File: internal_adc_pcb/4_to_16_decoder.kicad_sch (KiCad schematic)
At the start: 6 parts, among them U11 SN74AHC138RGYR, U12 SN74AHC138RGYR, U13 SN74LVC1G14DCKR_C19829630

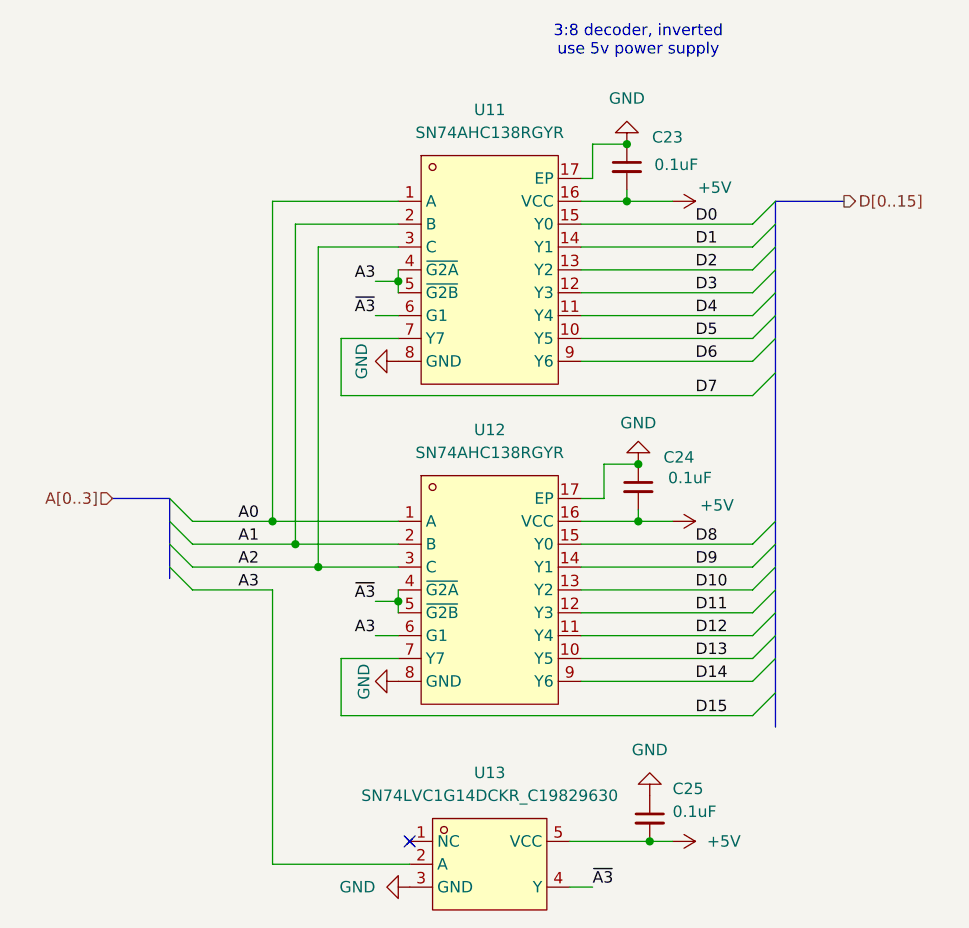
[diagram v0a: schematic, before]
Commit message: adjust VG issue for internal ADC version; changed naming for VG
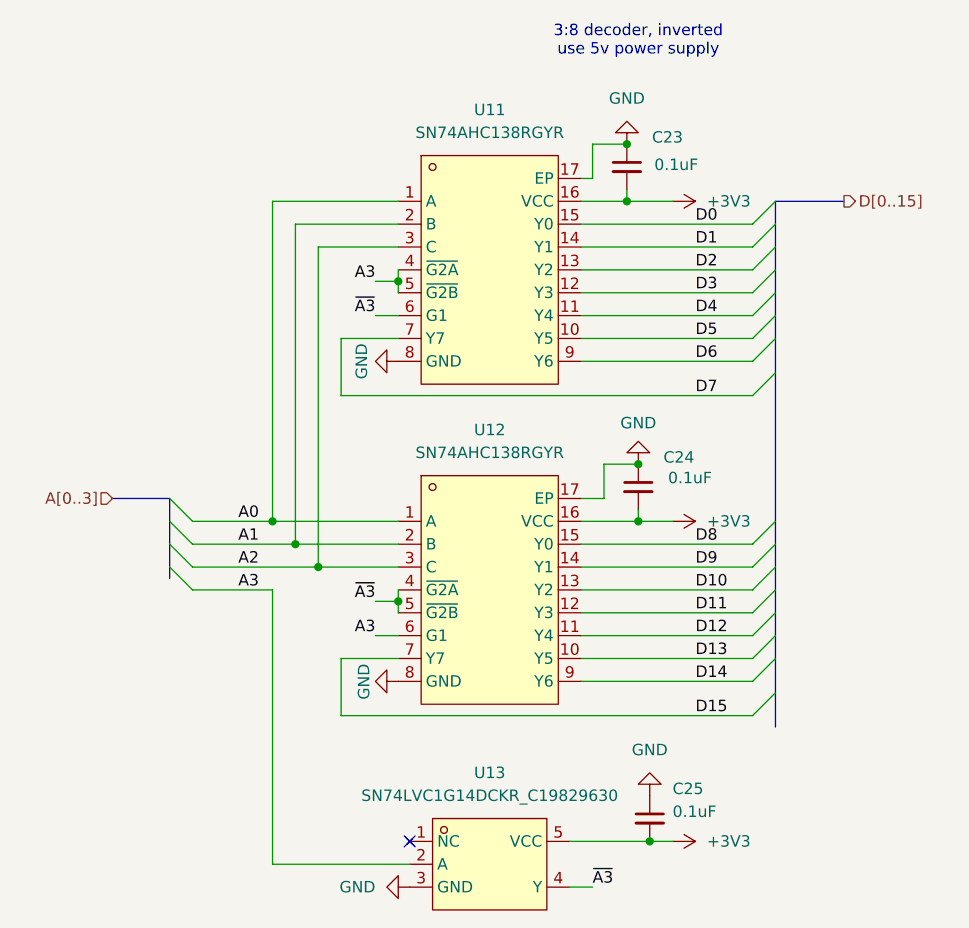
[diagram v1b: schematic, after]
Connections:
- net +5V renamed +3V3
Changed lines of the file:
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@@
 	)
 	(symbol
-		(lib_id "power:+5V")
-		(at 121.92 49.53 270)
-		(unit 1)
-		(body_style 1)
-		(exclude_from_sim no)
-		(in_bom yes)
-		(on_board yes)
-		(in_pos_files yes)
-		(dnp no)
-		(property "Reference" "#PWR065"
-			(at 118.11 49.53 0)
-			(hide yes)
-			(show_name no)
-			(do_not_autoplace no)
-			(effects
-				(font
-					(face "Iosevka NF")
-					(size 1.27 1.27)
-				)
-			)
-		)
-		(property "Value" "+5V"
-			(at 124.714 48.006 90)
-			(show_name no)
-			(do_not_autoplace no)
-			(effects
-				(font
-					(face "Iosevka NF")
+		(lib_id "power:+3V3")
+		(at 121.92 85.09 270)
+		(unit 1)
+		(body_style 1)
+		(exclude_from_sim no)
+		(in_bom yes)
+		(on_board yes)
+		(in_pos_files yes)
+		(dnp no)
+		(fields_autoplaced yes)
+		(property "Reference" "#PWR080"
+			(at 118.11 85.09 0)
+			(hide yes)
+			(show_name no)
+			(do_not_autoplace no)
+			(effects
+				(font
+					(size 1.27 1.27)
+				)
+			)
+		)
+		(property "Value" "+3V3"
+			(at 125.73 85.0899 90)
+			(show_name no)
+			(do_not_autoplace no)
+			(effects
+				(font
 					(size 1.27 1.27)
 				)
@@
 		)
 		(property "Footprint" ""
-			(at 121.92 49.53 0)
-			(hide yes)
-			(show_name no)
-			(do_not_autoplace no)
-			(effects
-				(font
-					(face "Iosevka NF")
-					(size 1.27 1.27)
-				)
-			)
-		)
-		(property "Datasheet" ""
-			(at 121.92 49.53 0)
-			(hide yes)
-			(show_name no)
-			(do_not_autoplace no)
-			(effects
-				(font
-					(face "Iosevka NF")
-					(size 1.27 1.27)
-				)
-			)
-		)
-		(property "Description" "Power symbol creates a global label with name \"+5V\""
-			(at 121.92 49.53 0)
-			(hide yes)
-			(show_name no)
-			(do_not_autoplace no)
-			(effects
-				(font
-					(face "Iosevka NF")
-					(size 1.27 1.27)
-				)
-			)
-		)
-		(pin "1"
-		)
-		(instances
-			(project "fsr_matrix_readout_external_adc"
-				(path "/6dca5e5c-f676-465d-98c9-14af6047a226/41800b67-536b-40f6-9870-7d633bd400f6"
-					(reference "#PWR02")
-					(unit 1)
-				)
-			)
-			(project "fsr_matrix_readout_internal_adc"
-				(path "/a2a8c34e-3adf-4a95-8857-b713f7048029/7bcd2658-0b6a-4321-9860-384b8d346995"
-					(reference "#PWR065")
+			(at 121.92 85.09 0)
+			(hide yes)
+			(show_name no)
+			(do_not_autoplace no)
+			(effects
+				(font
+					(size 1.27 1.27)
+				)
+			)
+		)
+		(property "Datasheet" ""
+			(at 121.92 85.09 0)
+			(hide yes)
+			(show_name no)
+			(do_not_autoplace no)
+			(effects
+				(font
+					(size 1.27 1.27)
+				)
+			)
+		)
+		(property "Description" "Power symbol creates a global label with name \"+3V3\""
+			(at 121.92 85.09 0)
+			(hide yes)
+			(show_name no)
+			(do_not_autoplace no)
+			(effects
+				(font
+					(size 1.27 1.27)
+				)
+			)
+		)
+		(pin "1"
+		)
+		(instances
+			(project "fsr_matrix_readout_internal_adc"
+				(path "/a2a8c34e-3adf-4a95-8857-b713f7048029/7bcd2658-0b6a-4321-9860-384b8d346995"
+					(reference "#PWR080")
 					(unit 1)
 				)
@@
 	)
 	(symbol
-		(lib_id "power:+5V")
-		(at 121.92 85.09 270)
-		(unit 1)
-		(body_style 1)
-		(exclude_from_sim no)
-		(in_bom yes)
-		(on_board yes)
-		(in_pos_files yes)
-		(dnp no)
-		(property "Reference" "#PWR066"
-			(at 118.11 85.09 0)
-			(hide yes)
-			(show_name no)
-			(do_not_autoplace no)
-			(effects
-				(font
-					(face "Iosevka NF")
-					(size 1.27 1.27)
-				)
-			)
-		)
-		(property "Value" "+5V"
-			(at 124.968 83.312 90)
-			(show_name no)
-			(do_not_autoplace no)
-			(effects
-				(font
-					(face "Iosevka NF")
-					(size 1.27 1.27)
-				)
-				(justify left)
-			)
-		)
-		(property "Footprint" ""
-			(at 121.92 85.09 0)
-			(hide yes)
-			(show_name no)
-			(do_not_autoplace no)
-			(effects
-				(font
-					(face "Iosevka NF")
-					(size 1.27 1.27)
-				)
-			)
-		)
-		(property "Datasheet" ""
-			(at 121.92 85.09 0)
-			(hide yes)
-			(show_name no)
-			(do_not_autoplace no)
-			(effects
-				(font
-					(face "Iosevka NF")
-					(size 1.27 1.27)
-				)
-			)
-		)
-		(property "Description" "Power symbol creates a global label with name \"+5V\""
-			(at 121.92 85.09 0)
-			(hide yes)
-			(show_name no)
-			(do_not_autoplace no)
-			(effects
-				(font
-					(face "Iosevka NF")
-					(size 1.27 1.27)
-				)
-			)
-		)
-		(pin "1"
-		)
-		(instances
-			(project "fsr_matrix_readout_external_adc"
-				(path "/6dca5e5c-f676-465d-98c9-14af6047a226/41800b67-536b-40f6-9870-7d633bd400f6"
-					(reference "#PWR01")
-					(unit 1)
-				)
-			)
-			(project "fsr_matrix_readout_internal_adc"
-				(path "/a2a8c34e-3adf-4a95-8857-b713f7048029/7bcd2658-0b6a-4321-9860-384b8d346995"
-					(reference "#PWR066")
-					(unit 1)
-				)
-			)
-		)
-	)
-	(symbol
-		(lib_id "power:+5V")
+		(lib_id "power:+3V3")
 		(at 121.92 120.65 270)
 		(unit 1)
@@
 			(effects
 				(font
-					(face "Iosevka NF")
-					(size 1.27 1.27)
-				)
-			)
-		)
-		(property "Value" "+5V"
+					(size 1.27 1.27)
+				)
+			)
+		)
+		(property "Value" "+3V3"
 			(at 125.73 120.6499 90)
 			(show_name no)
@@
 			(effects
 				(font
-					(face "Iosevka NF")
 					(size 1.27 1.27)
 				)
@@
 			(effects
 				(font
-					(face "Iosevka NF")
 					(size 1.27 1.27)
 				)
@@
 			(effects
 				(font
-					(face "Iosevka NF")
-					(size 1.27 1.27)
-				)
-			)
-		)
-		(property "Description" "Power symbol creates a global label with name \"+5V\""
+					(size 1.27 1.27)
+				)
+			)
+		)
+		(property "Description" "Power symbol creates a global label with name \"+3V3\""
 			(at 121.92 120.65 0)
 			(hide yes)
@@
 			(effects
 				(font
-					(face "Iosevka NF")
-					(size 1.27 1.27)
-				)
-			)
-		)
-		(pin "1"
-		)
-		(instances
-			(project "fsr_matrix_readout_external_adc"
-				(path "/6dca5e5c-f676-465d-98c9-14af6047a226/41800b67-536b-40f6-9870-7d633bd400f6"
-					(reference "#PWR03")
-					(unit 1)
-				)
-			)
+					(size 1.27 1.27)
+				)
+			)
+		)
+		(pin "1"
+		)
+		(instances
 			(project "fsr_matrix_readout_internal_adc"
 				(path "/a2a8c34e-3adf-4a95-8857-b713f7048029/7bcd2658-0b6a-4321-9860-384b8d346995"
@@
 					(unit 1)
 				)
+			)
+		)
+	)
+	(symbol
+		(lib_id "power:+3V3")
+		(at 121.92 49.53 270)
+		(unit 1)
+		(body_style 1)
+		(exclude_from_sim no)
+		(in_bom yes)
+		(on_board yes)
+		(in_pos_files yes)
+		(dnp no)
+		(fields_autoplaced yes)
+		(property "Reference" "#PWR081"
+			(at 118.11 49.53 0)
+			(hide yes)
+			(show_name no)
+			(do_not_autoplace no)
+			(effects
+				(font
+					(size 1.27 1.27)
+				)
+			)
+		)
+		(property "Value" "+3V3"
+			(at 125.73 49.5299 90)
+			(show_name no)
+			(do_not_autoplace no)
+			(effects
+				(font
+					(size 1.27 1.27)
+				)
+				(justify left)
+			)
+		)
+		(property "Footprint" ""
+			(at 121.92 49.53 0)
+			(hide yes)
+			(show_name no)
+			(do_not_autoplace no)
+			(effects
+				(font
+					(size 1.27 1.27)
+				)
+			)
+		)
+		(property "Datasheet" ""
+			(at 121.92 49.53 0)
+			(hide yes)
+			(show_name no)
+			(do_not_autoplace no)
+			(effects
+				(font
+					(size 1.27 1.27)
+				)
+			)
+		)
+		(property "Description" "Power symbol creates a global label with name \"+3V3\""
+			(at 121.92 49.53 0)
+			(hide yes)
+			(show_name no)
+			(do_not_autoplace no)
+			(effects
+				(font
+					(size 1.27 1.27)
+				)
+			)
+		)
+		(pin "1"
+		)
+		(instances
+			(project "fsr_matrix_readout_internal_adc"
+				(path "/a2a8c34e-3adf-4a95-8857-b713f7048029/7bcd2658-0b6a-4321-9860-384b8d346995"
+					(reference "#PWR081")
+					(unit 1)
+				)

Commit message: update pcb for internal adc version
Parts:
- C23, C24, C25: footprint (none) -> Capacitor_SMD:C_0603_1608Metric
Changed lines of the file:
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@@
 			)
 		)
-		(property "Footprint" ""
+		(property "Footprint" "Capacitor_SMD:C_0603_1608Metric"
 			(at 119.38 118.11 0)
 			(hide yes)
@@
 			)
 		)
-		(property "Footprint" ""
+		(property "Footprint" "Capacitor_SMD:C_0603_1608Metric"
 			(at 116.84 45.72 0)
 			(hide yes)
@@
 			)
 		)
-		(property "Footprint" ""
+		(property "Footprint" "Capacitor_SMD:C_0603_1608Metric"
 			(at 118.11 81.28 0)
 			(hide yes)

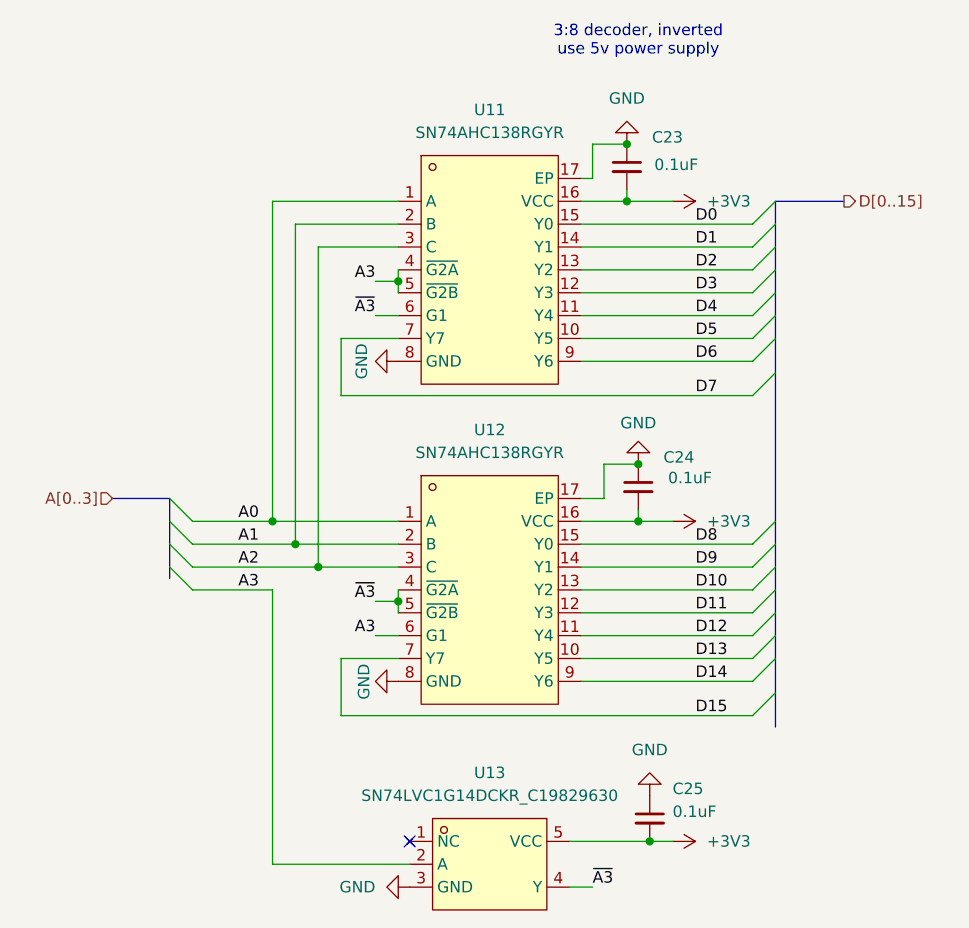
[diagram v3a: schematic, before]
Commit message: fixing all ERC errors for internal ADC ver, fixing warnings now
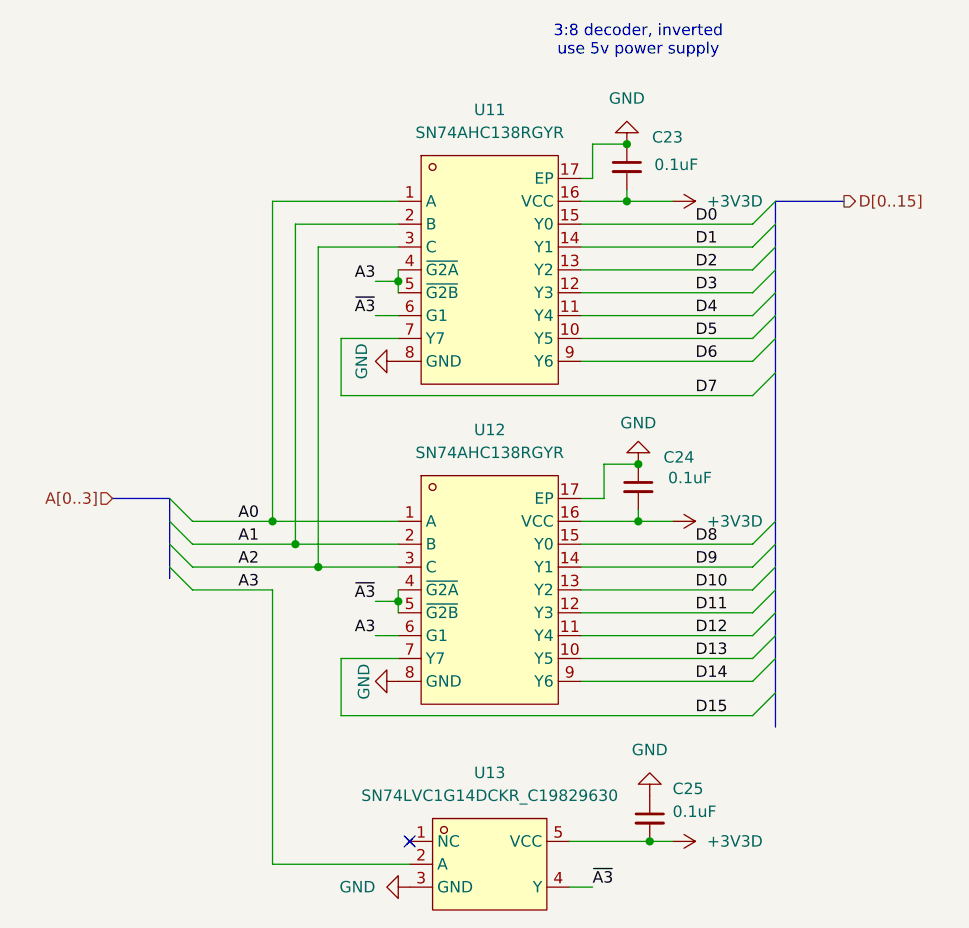
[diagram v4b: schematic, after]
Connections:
- net +3V3 renamed +3V3D
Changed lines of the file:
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@@
 			)
 		)
-		(property "Value" "+3V3"
+		(property "Value" "+3V3D"
 			(at 125.73 85.0899 90)
 			(show_name no)
@@
 			)
 		)
-		(property "Value" "+3V3"
+		(property "Value" "+3V3D"
 			(at 125.73 120.6499 90)
 			(show_name no)
@@
 			)
 		)
-		(property "Value" "+3V3"
+		(property "Value" "+3V3D"
 			(at 125.73 49.5299 90)
 			(show_name no)
